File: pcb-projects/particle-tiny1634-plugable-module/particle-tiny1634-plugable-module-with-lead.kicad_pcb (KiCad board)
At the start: 2 copper layers, 41.3 x 47.6 mm, 32 parts, among them IC1 ATTINY1634-SU, P1 INTERFACE, P2 MCU_TEST

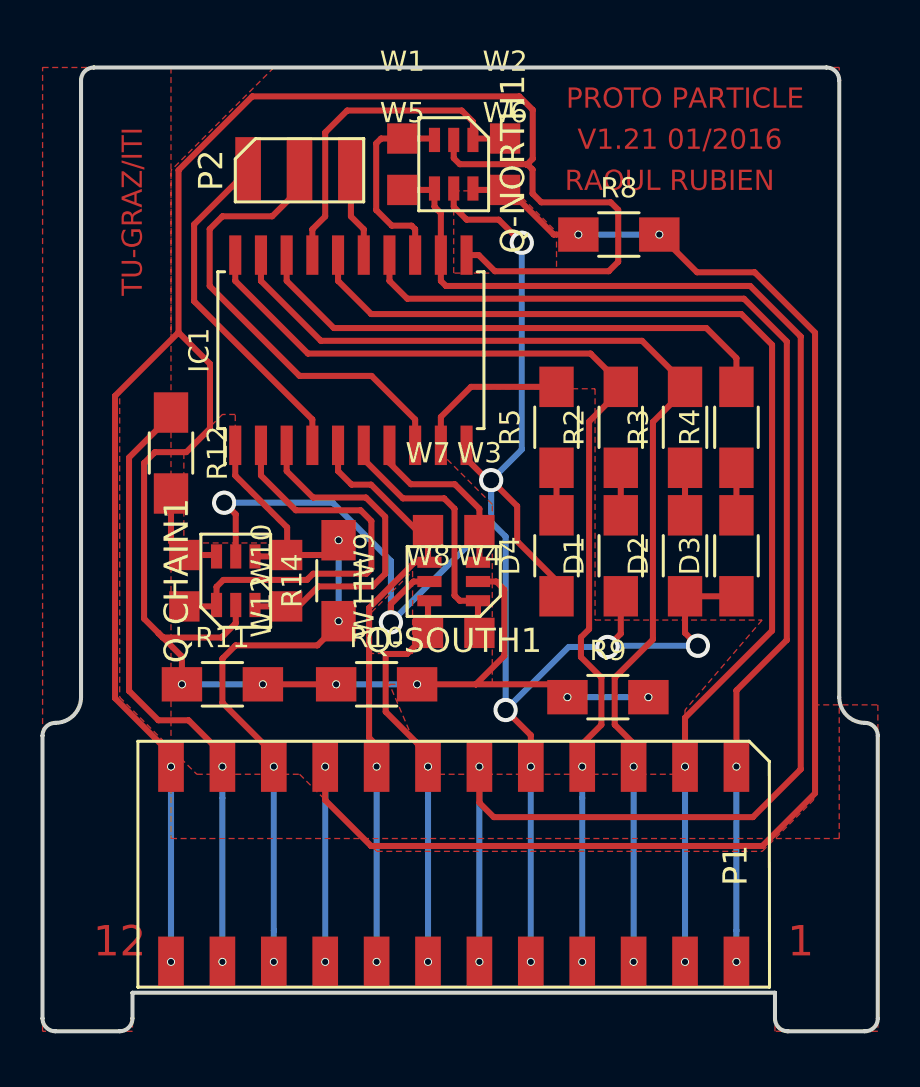
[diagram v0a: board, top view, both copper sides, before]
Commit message: remved no-net zones, refined gnd zone
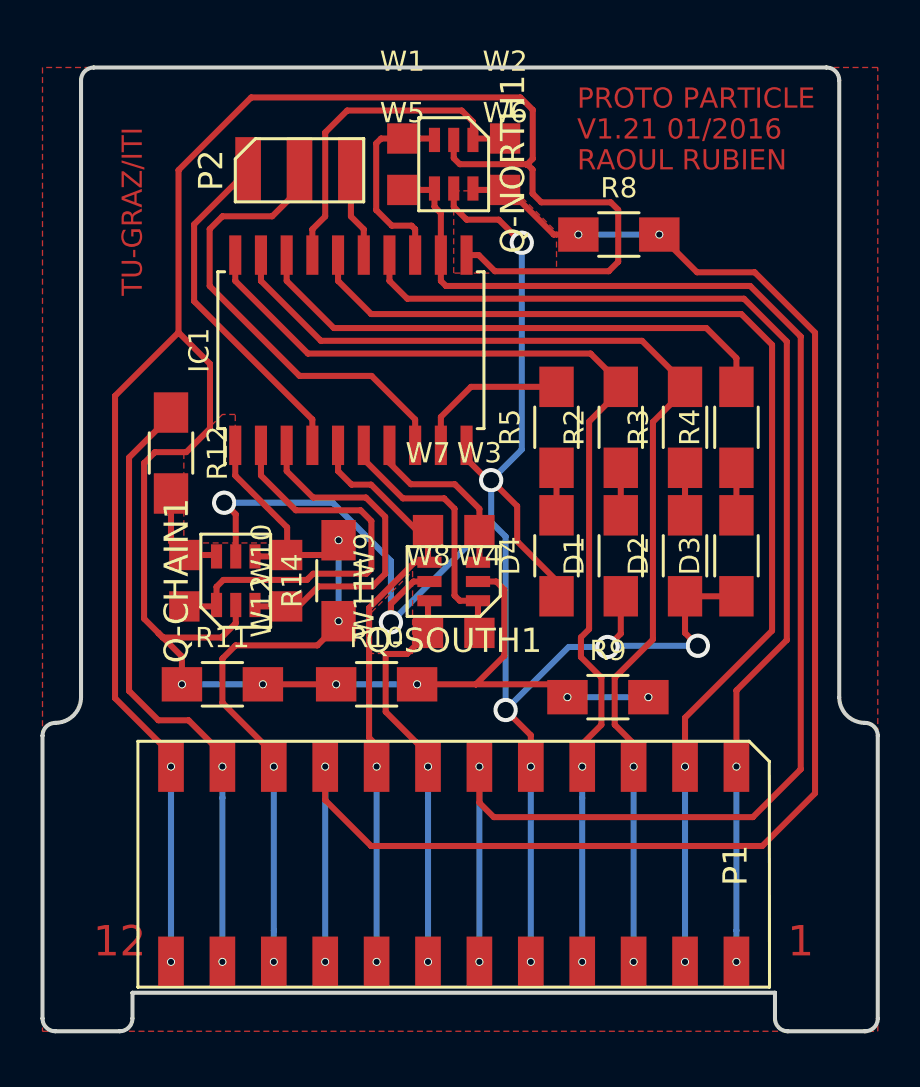
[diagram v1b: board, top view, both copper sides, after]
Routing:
- removed copper zone on F.Cu, net (none)
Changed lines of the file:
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@@
     (links 77)
     (no_connects 0)
-    (area 123.286787 76.525 180.085 147.520001)
+    (area 126.899999 83.719999 168.375001 131.545001)
     (thickness 1.6)
     (drawings 32)
@@
     (last_trace_width 0.3)
     (trace_clearance 0.33)
-    (zone_clearance 0.508)
+    (zone_clearance 0.33)
     (zone_45_only no)
     (trace_min 0.2)
@@
     (effects (font (size 1.5 1.5) (thickness 0.3)))
   )
-  (gr_text "RAOUL RUBIEN" (at 157.988 89.408) (layer F.Cu)
-    (effects (font (size 1 1) (thickness 0.2)))
+  (gr_text "RAOUL RUBIEN  " (at 153.416 88.392) (layer F.Cu)
+    (effects (font (size 1 1) (thickness 0.2)) (justify left))
   )
   (gr_text TU-GRAZ/ITI (at 131.445 90.932 90) (layer F.Cu)
     (effects (font (size 1 1) (thickness 0.2)))
   )
-  (gr_text "V1.21 01/2016" (at 158.496 87.376) (layer F.Cu)
-    (effects (font (size 1 1) (thickness 0.2)))
-  )
-  (gr_text "PROTO PARTICLE" (at 158.75 85.344) (layer F.Cu)
-    (effects (font (size 1 1) (thickness 0.2)))
+  (gr_text "V1.21 01/2016 " (at 153.416 86.868) (layer F.Cu)
+    (effects (font (size 1 1) (thickness 0.2)) (justify left))
+  )
+  (gr_text "PROTO PARTICLE" (at 153.416 85.344) (layer F.Cu)
+    (effects (font (size 1 1) (thickness 0.2)) (justify left))
   )
   (dimension 47.625 (width 0.3) (layer Dwgs.User)
@@
   (segment (start 146.685 101.088) (end 148.173 99.6) (width 0.3) (layer F.Cu) (net 16))
   (segment (start 148.173 99.6) (end 152.4 99.6) (width 0.3) (layer F.Cu) (net 16) (status 20))
+  (segment (start 150.955142 88.6) (end 151.224857 88.330285) (width 0.3) (layer F.Cu) (net 17))
+  (segment (start 150.612634 85.300464) (end 137.312204 85.300464) (width 0.3) (layer F.Cu) (net 17))
+  (segment (start 151.224857 88.330285) (end 151.224857 85.912687) (width 0.3) (layer F.Cu) (net 17))
+  (segment (start 151.224857 85.912687) (end 150.612634 85.300464) (width 0.3) (layer F.Cu) (net 17))
+  (segment (start 137.312204 85.300464) (end 133.721869 88.890799) (width 0.3) (layer F.Cu) (net 17))
+  (segment (start 133.721869 88.890799) (end 133.721869 96.910131) (width 0.3) (layer F.Cu) (net 17))
   (segment (start 133.35 128.015) (end 133.35 118.365) (width 0.3) (layer B.Cu) (net 17))
   (segment (start 152.94 114.935) (end 156.94 114.935) (width 0.3) (layer B.Cu) (net 17))
@@
   (segment (start 145.51 114.3) (end 148.415142 114.3) (width 0.3) (layer F.Cu) (net 17) (status 10))
   (segment (start 148.415142 114.3) (end 149.820571 112.894571) (width 0.3) (layer F.Cu) (net 17))
-  (segment (start 150.955142 88.6) (end 151.224857 88.330285) (width 0.3) (layer F.Cu) (net 17))
-  (segment (start 151.224857 88.330285) (end 151.224857 85.912687) (width 0.3) (layer F.Cu) (net 17))
-  (segment (start 151.224857 85.912687) (end 150.560481 85.248311) (width 0.3) (layer F.Cu) (net 17))
-  (segment (start 150.560481 85.248311) (end 137.364357 85.248311) (width 0.3) (layer F.Cu) (net 17))
-  (segment (start 137.364357 85.248311) (end 133.721869 88.890799) (width 0.3) (layer F.Cu) (net 17))
-  (segment (start 133.721869 88.890799) (end 133.721869 96.910131) (width 0.3) (layer F.Cu) (net 17))
   (segment (start 137.89 114.3) (end 141.51 114.3) (width 0.3) (layer F.Cu) (net 17) (status 30))
   (segment (start 136.549429 110.380571) (end 136.549429 111.280571) (width 0.3) (layer F.Cu) (net 17) (status 10))
@@
     (polygon
       (pts
-        (xy 165.104807 115.316) (xy 168.279807 115.316) (xy 168.279807 131.445) (xy 163.195 131.445) (xy 163.195 129.54)
-        (xy 131.445 129.54) (xy 131.445 131.445) (xy 127.004807 131.445) (xy 127.004807 83.82) (xy 138.434807 83.82)
-        (xy 133.354807 88.9) (xy 133.354807 97.155) (xy 130.814807 99.695) (xy 130.814807 114.935) (xy 134.624807 118.745)
-        (xy 139.704807 118.745) (xy 143.514807 122.555) (xy 162.564807 122.555) (xy 165.104807 120.015)
-      )
-    )
-  )
-  (zone (net 1) (net_name GND) (layer F.Cu) (hatch edge 0.508)
-    (priority 1)
-    (connect_pads (clearance 0.508))
-    (min_thickness 0.254)
-    (fill yes (arc_segments 16) (thermal_gap 0.508) (thermal_bridge_width 0.508))
-    (polygon
-      (pts
-        (xy 146.685 100.965) (xy 147.955 99.695) (xy 154.305 99.695) (xy 154.305 111.125) (xy 162.56 111.125)
-        (xy 158.75 115.57) (xy 158.75 118.745) (xy 146.05 118.745) (xy 144.145 114.3) (xy 149.225 114.3)
-        (xy 149.225 105.41) (xy 146.685 102.87)
-      )
-    )
-  )
-  (zone (net 1) (net_name GND) (layer F.Cu) (hatch edge 0.508)
-    (priority 1)
-    (connect_pads (clearance 0.508))
-    (min_thickness 0.254)
-    (fill yes (arc_segments 16) (thermal_gap 0.508) (thermal_bridge_width 0.508))
-    (polygon
-      (pts
         (xy 135.89 100.965) (xy 133.985 102.87) (xy 133.985 107.315) (xy 139.065 107.315) (xy 139.065 106.68)
         (xy 136.525 104.14) (xy 136.525 100.965)
@@
     )
   )
-  (zone (net 0) (net_name "") (layer F.Cu) (hatch edge 0.508)
-    (connect_pads (clearance 0.508))
-    (min_thickness 0.254)
-    (fill yes (arc_segments 16) (thermal_gap 0.508) (thermal_bridge_width 0.508))
+  (zone (net 1) (net_name GND) (layer F.Cu) (hatch edge 0.508)
+    (connect_pads (clearance 0.33))
+    (min_thickness 0.3)
+    (fill yes (arc_segments 32) (thermal_gap 0.508) (thermal_bridge_width 0.508))
     (polygon
       (pts
-        (xy 133.35 121.92) (xy 166.37 121.92) (xy 166.37 83.82) (xy 133.35 83.82)
+        (xy 127 131.445) (xy 168.275 131.445) (xy 168.275 83.82) (xy 127 83.82)
       )
     )

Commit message: added power supply capacitor
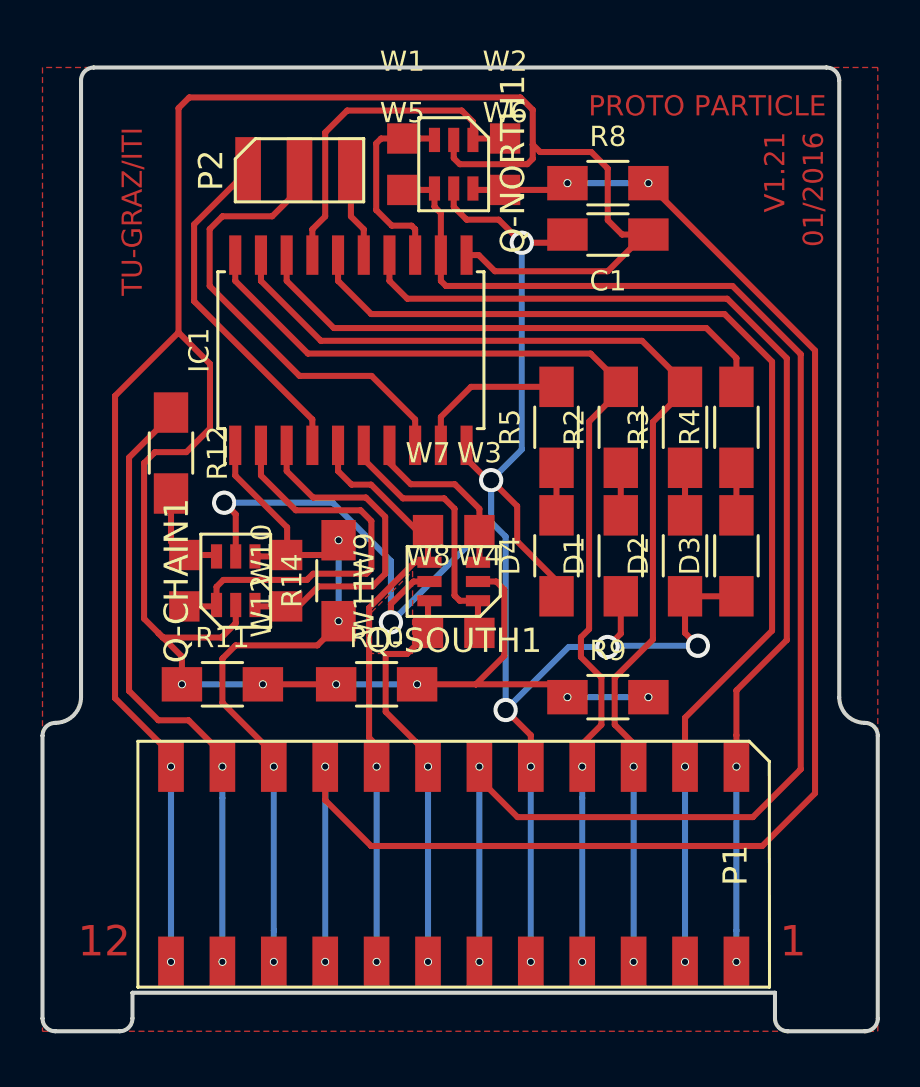
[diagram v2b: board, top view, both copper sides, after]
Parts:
- added C1: 100nF, Capacitors_SMD:C_1206_HandSoldering, F.Cu at (154.9, 92.1)
- moved R8 2.60 mm to (154.9, 89.5)
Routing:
- net VCC: track 141.2 -> 145.4 mm
- net GND: track 95.8 -> 98.3 mm
- net /RX-NORTH: track 75.2 -> 74.0 mm
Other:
- board text added: "01/2016"
- board text added: "V1.21"
- board text removed: "RAOUL RUBIEN"
- board text removed: "V1.21 01/2016"
